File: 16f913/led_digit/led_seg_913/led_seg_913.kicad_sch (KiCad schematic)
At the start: 33 parts, among them IC1 PIC16873P P16f913, J1 MTA06-156, Q1 20.0MHz, T1 BC337, T2 BC337, T3 BC337, T4 BC337, T5 BC337, U1 CC56-12EWA, U2 HDSP-7501

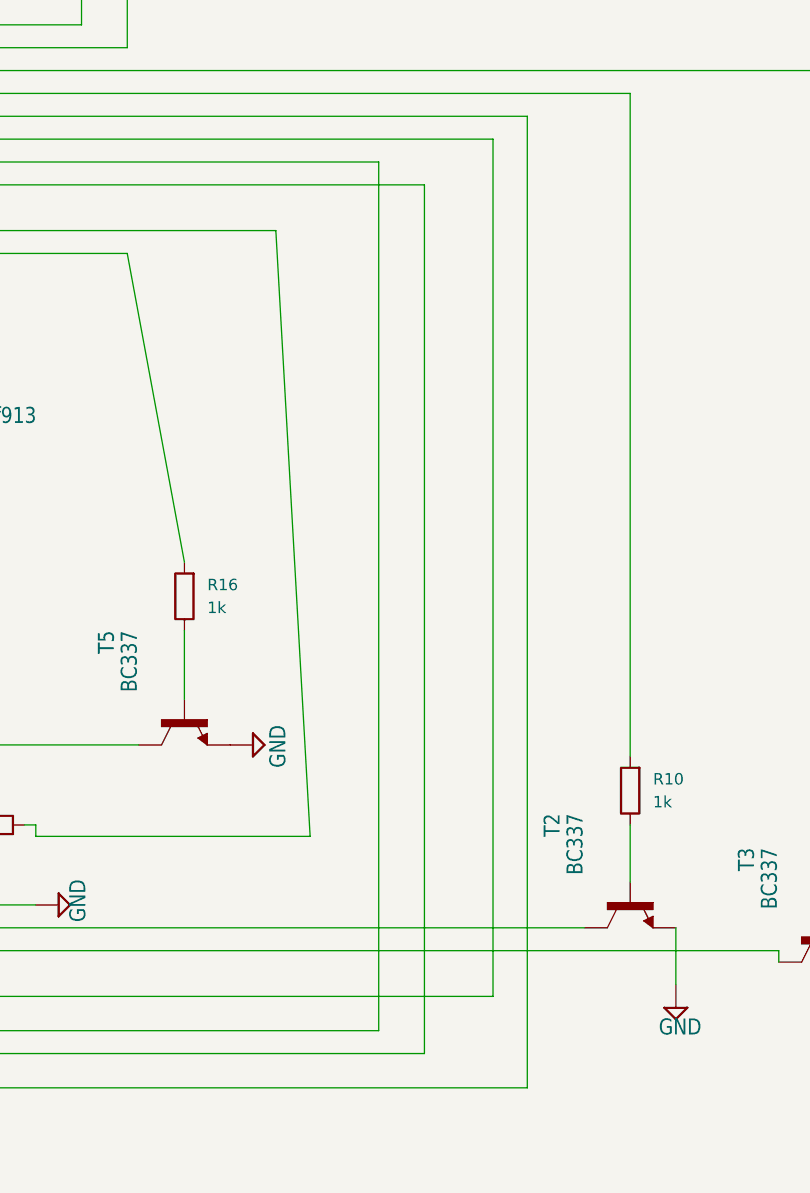
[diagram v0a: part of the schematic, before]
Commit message: pic16f84a led digit segments usage example prepared from different modules simple every 1 sec value increment 10 MHz osc
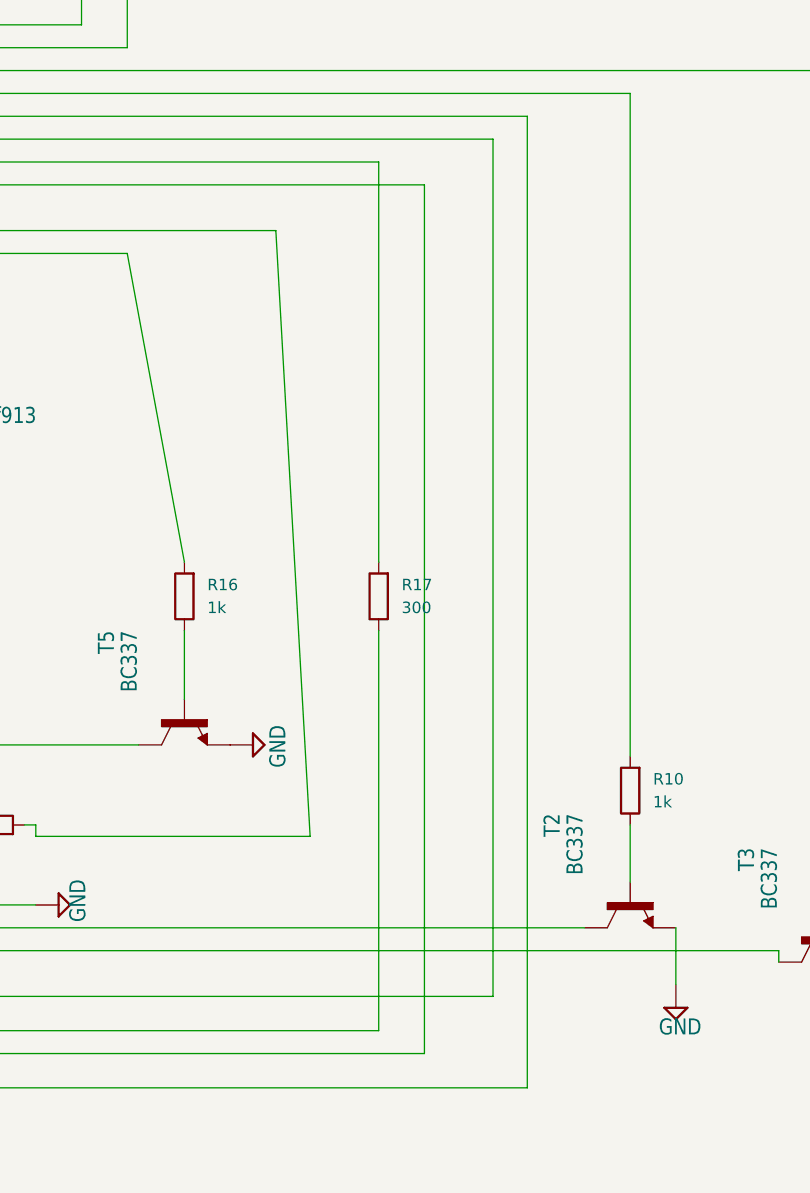
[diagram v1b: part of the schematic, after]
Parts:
- added R17: 300, symbol Device:R
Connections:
- net at U1.10 (f): now also R17.1; no longer IC1.22 (RB1)
- new net: IC1.22 (RB1), R17.2
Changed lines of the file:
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@@
+	(wire
+		(pts
+			(xy 232.41 179.07) (xy 232.41 134.62)
+		)
+		(stroke
+			(width 0)
+			(type default)
+		)
+	)
 	(wire
 		(pts
@@
 	(wire
 		(pts
-			(xy 232.41 231.14) (xy 232.41 134.62)
+			(xy 232.41 231.14) (xy 232.41 186.69)
 		)
 		(stroke
@@
 					(unit 1)
 				)
+			)
+		)
+	)
+	(symbol
+		(lib_id "Device:R")
+		(at 232.41 182.88 180)
+		(unit 1)
+		(exclude_from_sim no)
+		(in_bom yes)
+		(on_board yes)
+		(dnp no)
+		(fields_autoplaced yes)
+		(property "Reference" "R17"
+			(at 234.95 181.6099 0)
+			(effects
+				(font
+					(size 1.27 1.27)
+				)
+				(justify right)
+			)
+		)
+		(property "Value" "300"
+			(at 234.95 184.1499 0)
+			(effects
+				(font
+					(size 1.27 1.27)
+				)
+				(justify right)
+			)
+		)
+		(property "Footprint" ""
+			(at 234.188 182.88 90)
+			(effects
+				(font
+					(size 1.27 1.27)
+				)
+				(hide yes)
+			)
+		)
+		(property "Datasheet" "~"
+			(at 232.41 182.88 0)
+			(effects
+				(font
+					(size 1.27 1.27)
+				)
+				(hide yes)
+			)
+		)
+		(property "Description" ""
+			(at 232.41 182.88 0)
+			(effects
+				(font
+					(size 1.27 1.27)
+				)
+			)
+		)
+		(pin "1"
+		)
+		(pin "2"
+		)
+		(instances
+			(project "led_seg_913"
+				(path "/841da6f7-1698-4810-a4eb-50d82cc331bc"
+					(reference "R17")
+					(unit 1)
+				)
